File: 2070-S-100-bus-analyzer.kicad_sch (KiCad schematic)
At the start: 90 parts, among them J1 S-100 Edge Connector, J10 Conn_02x13_Odd_Even, J11 Conn_02x13_Odd_Even, J12 USB4105-GF-A, J13 Conn_01x01, J14 Conn_01x01, J15 Conn_01x02, J16 Conn_01x02, J17 Conn_01x02, J18 Conn_01x02, J19 Conn_01x02, J2 Conn_02x13_Odd_Even, J3 Conn_02x13_Odd_Even, J4 Conn_02x13_Odd_Even, J5 Conn_02x13_Odd_Even, J6 Conn_02x13_Odd_Even, J7 Conn_02x13_Odd_Even, J8 Conn_02x13_Odd_Even, J9 Conn_02x13_Odd_Even, SW1 SW_MEC_5E, U1 74LVCH245APW,118, U10 74LVCH245APW,118, U11 74LVCH245APW,118, U12 74LVCH245APW,118, U13 74LVCH245APW,118, U14 74LVCH245APW,118, U15 74LVCH245APW,118, U16 AP63300, U17 LMS78_05-2.0R, U2 74LVCH245APW,118, U3 74LVCH245APW,118, U4 74LVCH245APW,118, U5 74LVCH245APW,118, U6 74LVCH245APW,118, U7 74LVCH245APW,118, U8 74LVCH245APW,118, U9 74LVCH245APW,118

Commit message: Add some part info
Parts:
- R11: Digi-Key_PN (none) -> 311-2.20KHRCT-ND
- R4, R5: Digi-Key_PN (none) -> CR0603-FX-510ELFCT-ND
- TP1, TP2: Digi-Key_PN (none) -> 2019-RCWCTECT-ND
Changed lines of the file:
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@@
 			)
 		)
-		(property "Digi-Key_PN" ""
+		(property "Digi-Key_PN" "2019-RCWCTECT-ND"
 			(at 293.37 49.53 0)
 			(effects
@@
 			)
 		)
-		(property "Digi-Key_PN" ""
+		(property "Digi-Key_PN" "311-2.20KHRCT-ND"
 			(at 411.48 36.83 0)
 			(effects
@@
 			)
 		)
-		(property "Digi-Key_PN" ""
+		(property "Digi-Key_PN" "CR0603-FX-510ELFCT-ND"
 			(at 473.71 360.68 0)
 			(effects
@@
 			)
 		)
-		(property "Digi-Key_PN" ""
+		(property "Digi-Key_PN" "CR0603-FX-510ELFCT-ND"
 			(at 473.71 363.22 0)
 			(effects
@@
 			)
 		)
-		(property "Digi-Key_PN" ""
+		(property "Digi-Key_PN" "2019-RCWCTECT-ND"
 			(at 275.59 49.53 0)
 			(effects

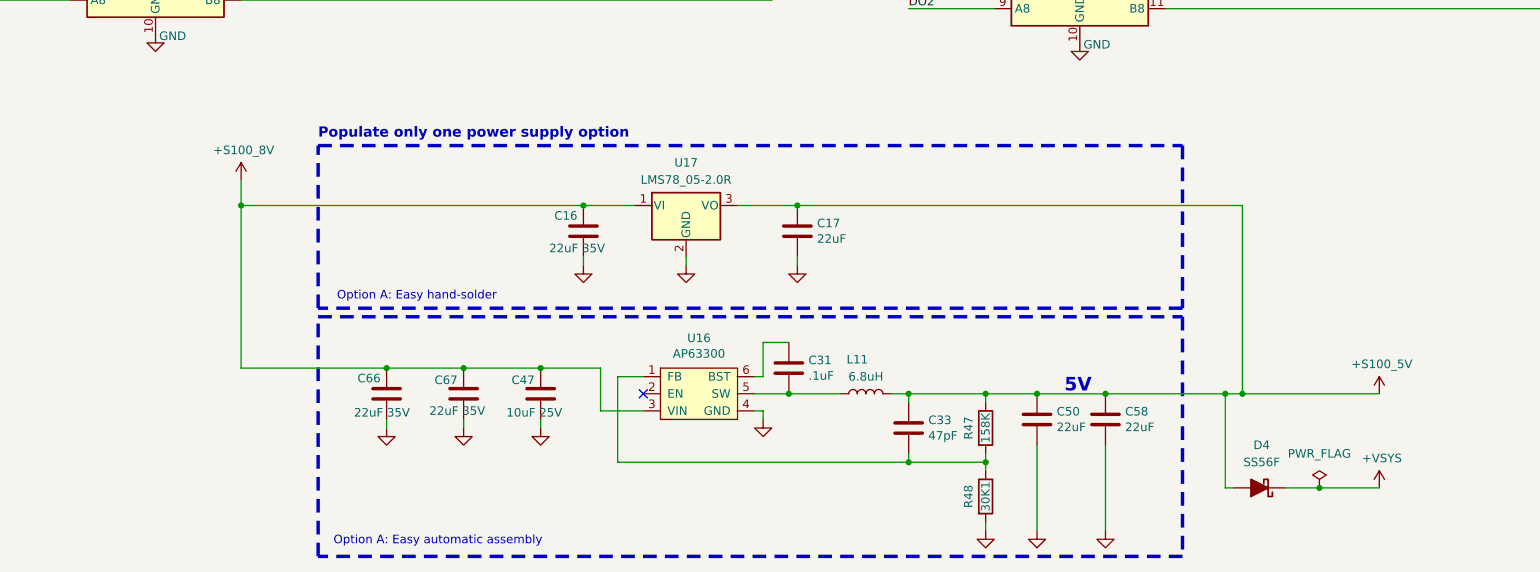
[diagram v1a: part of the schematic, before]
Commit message: Remove linear regulator option
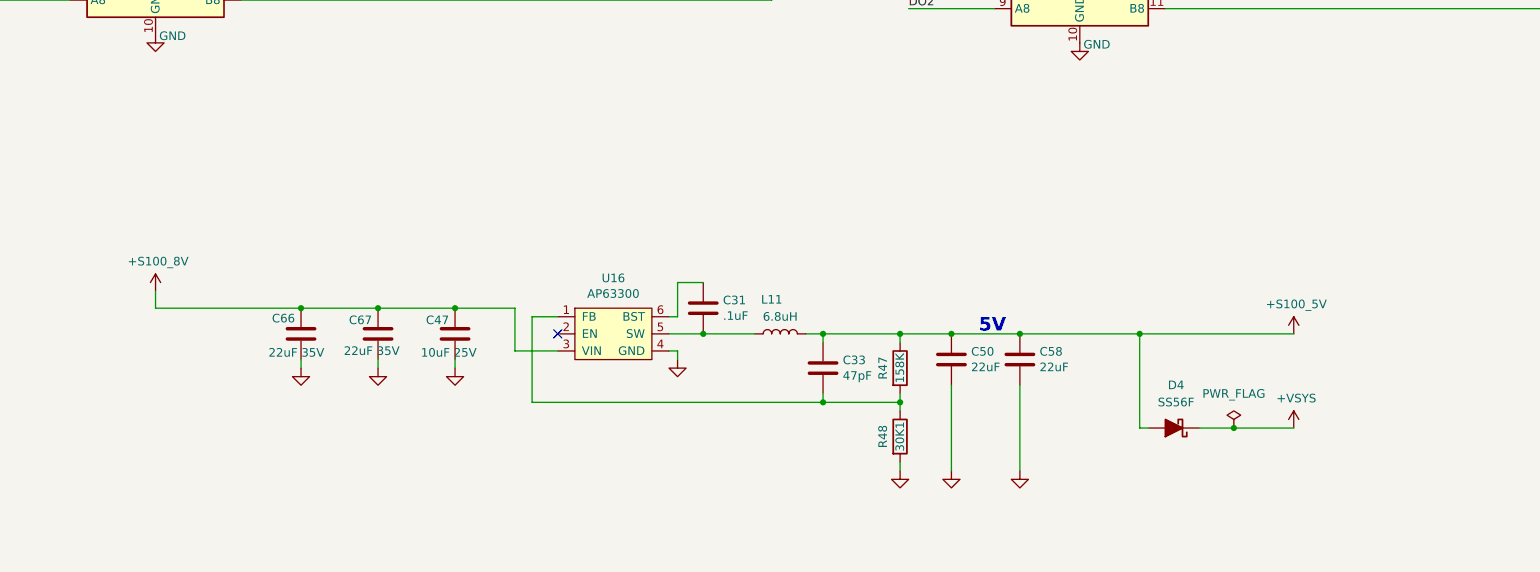
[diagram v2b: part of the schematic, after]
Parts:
- removed C16: 22uF 35V, Capacitor_SMD:C_0805_2012Metric_Pad1.18x1.45mm_HandSolder, symbol Device:C
- removed C17: 22uF, Capacitor_SMD:C_0805_2012Metric_Pad1.18x1.45mm_HandSolder, symbol Device:C
- removed U17: LMS78_05-2.0R, Package_TO_SOT_THT:TO-220-3_Horizontal_TabDown, symbol Regulator_Linear:LM7805_TO220
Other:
- note removed: "Option A: Easy automatic assembly"
- note removed: "Option A: Easy hand-solder"
- note removed: "Populate only one power supply option"
- moved on the sheet: C31, C33, C47, C50, C58, C66, C67, D4, L11, R47, R48, U16

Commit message: Add 3rd header row, note pins20/70, fonts, BOM
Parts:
- removed J13, J14: Conn_01x01, Connector_PinHeader_2.54mm:PinHeader_1x01_P2.54mm_Vertical, symbol Connector_Generic:Conn_01x01
- added J13, J14: Conn_01x02, Connector_PinHeader_2.54mm:PinHeader_1x02_P2.54mm_Vertical, symbol Connector_Generic:Conn_01x02
- added J22, J23, J24, J25, J26, J27, J28, J29: Conn_01x13, Connector_PinHeader_2.54mm:PinHeader_1x13_P2.54mm_Vertical, symbol Connector_Generic:Conn_01x13
- R11: MPN (none) -> RC0603FR-072K2L; Manufacturer (none) -> YAGEO
- R4, R5: MPN (none) -> CR0603-FX-5110ELF; Manufacturer (none) -> Bourns Inc.
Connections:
- net GND: now also J13.2 (Pin_2), J14.2 (Pin_2), J22.13 (Pin_13), J23.13 (Pin_13), J24.13 (Pin_13), J25.12 (Pin_12), J25.13 (Pin_13), J26.13 (Pin_13), J27.13 (Pin_13), J28.13 (Pin_13), J29.12 (Pin_12), J29.13 (Pin_13)
- net at J1.3 (XRDY), J2.1 (Pin_1): now also J22.1 (Pin_1)
- net at J1.8 (~{VI4}), J2.11 (Pin_11): now also J22.6 (Pin_6)
- net at J1.9 (~{VI5}), J2.13 (Pin_13): now also J22.7 (Pin_7)
- net at J1.10 (~{VI6}), J2.15 (Pin_15): now also J22.8 (Pin_8)
- net at J1.11 (~{VI7}), J2.17 (Pin_17): now also J22.9 (Pin_9)
- net at J1.12 (~{NMI}), J2.19 (Pin_19): now also J22.10 (Pin_10)
- net at J1.13 (~{PWRFAIL}), J2.21 (Pin_21): now also J22.11 (Pin_11)
- net at J1.14 (~{DMA3}), J2.23 (Pin_23): now also J22.12 (Pin_12)
- net at J1.4 (~{VI0}), J2.3 (Pin_3): now also J22.2 (Pin_2)
- net at J1.5 (~{VI1}), J2.5 (Pin_5): now also J22.3 (Pin_3)
- net at J1.6 (~{VI2}), J2.7 (Pin_7): now also J22.4 (Pin_4)
- net at J1.7 (~{VI3}), J2.9 (Pin_9): now also J22.5 (Pin_5)
- net at J1.15 (A18), J3.1 (Pin_1): now also J23.1 (Pin_1)
- net at J1.16 (A16), J3.3 (Pin_3): now also J23.2 (Pin_2)
- net at J1.17 (A17), J3.5 (Pin_5): now also J23.3 (Pin_3)
- net at J1.18 (~{SDSB}), J3.7 (Pin_7): now also J23.4 (Pin_4)
- net at J1.19 (~{CDSB}), J3.9 (Pin_9): now also J23.5 (Pin_5)
- net S100_20: now reaches J1.20 (GND), J3.11 (Pin_11)
- net S100_20: now also J14.1 (Pin_1), J23.6 (Pin_6)
- net at J1.21 (NDEF), J3.13 (Pin_13): now also J23.7 (Pin_7)
- net at J1.22 (~{ADSB}), J3.15 (Pin_15): now also J23.8 (Pin_8)
- net at J1.23 (~{DODSB}), J3.17 (Pin_17): now also J23.9 (Pin_9)
- net at J1.24 (PHI), J3.19 (Pin_19): now also J23.10 (Pin_10)
- net at J1.25 (~{pSTVAL}), J3.21 (Pin_21): now also J23.11 (Pin_11)
- net at J1.26 (pHLDA), J3.23 (Pin_23): now also J23.12 (Pin_12)
- net at J1.27 (RFU), J4.1 (Pin_1): now also J24.1 (Pin_1)
- net at J1.28 (RFU), J4.3 (Pin_3): now also J24.2 (Pin_2)
- net at J1.29 (A5), J4.5 (Pin_5): now also J24.3 (Pin_3)
- net at J1.30 (A4), J4.7 (Pin_7): now also J24.4 (Pin_4)
- net at J1.31 (A3), J4.9 (Pin_9): now also J24.5 (Pin_5)
- net at J1.32 (A15), J4.11 (Pin_11): now also J24.6 (Pin_6)
- net at J1.33 (A12), J4.13 (Pin_13): now also J24.7 (Pin_7)
- net at J1.34 (A9), J4.15 (Pin_15): now also J24.8 (Pin_8)
- net at J1.35 (DO1), J4.17 (Pin_17): now also J24.9 (Pin_9)
- net at J1.36 (DO0), J4.19 (Pin_19): now also J24.10 (Pin_10)
- net at J1.37 (A10), J4.21 (Pin_21): now also J24.11 (Pin_11)
- net at J1.38 (DO4), J4.23 (Pin_23): now also J24.12 (Pin_12)
- net at J1.39 (DO5), J5.1 (Pin_1): now also J25.1 (Pin_1)
- net at J1.40 (DO6), J5.3 (Pin_3): now also J25.2 (Pin_2)
- net at J1.41 (DI2), J5.5 (Pin_5): now also J25.3 (Pin_3)
- net at J1.42 (DI3), J5.7 (Pin_7): now also J25.4 (Pin_4)
- net at J1.43 (DI7), J5.9 (Pin_9): now also J25.5 (Pin_5)
- net at J1.44 (sM1), J5.11 (Pin_11): now also J25.6 (Pin_6)
- net at J1.45 (sOUT), J5.13 (Pin_13): now also J25.7 (Pin_7)
- net at J1.46 (sINP), J5.15 (Pin_15): now also J25.8 (Pin_8)
- net at J1.47 (sMEMR), J5.17 (Pin_17): now also J25.9 (Pin_9)
- net at J1.48 (sHLTA), J5.19 (Pin_19): now also J25.10 (Pin_10)
- net at J1.49 (CLOCK), J5.21 (Pin_21): now also J25.11 (Pin_11)
- net at J1.53 (GND), J6.1 (Pin_1): now also J26.1 (Pin_1)
- net at J1.54 (~{SLV_CLR}), J6.3 (Pin_3): now also J26.2 (Pin_2)
- net at J1.55 (~{DMA0}), J6.5 (Pin_5): now also J26.3 (Pin_3)
- net at J1.56 (~{DMA1}), J6.7 (Pin_7): now also J26.4 (Pin_4)
- net at J1.57 (~{DMA2}), J6.9 (Pin_9): now also J26.5 (Pin_5)
- net at J1.58 (~{sXTRQ}), J6.11 (Pin_11): now also J26.6 (Pin_6)
- net at J1.59 (A19), J6.13 (Pin_13): now also J26.7 (Pin_7)
- net at J1.60 (~{SIXTN}), J6.15 (Pin_15): now also J26.8 (Pin_8)
- net at J1.61 (A20), J6.17 (Pin_17): now also J26.9 (Pin_9)
- net at J1.62 (A21), J6.19 (Pin_19): now also J26.10 (Pin_10)
- net at J1.63 (A22), J6.21 (Pin_21): now also J26.11 (Pin_11)
- net at J1.64 (A23), J6.23 (Pin_23): now also J26.12 (Pin_12)
- net at J1.65 (NDEF), J7.1 (Pin_1): now also J27.1 (Pin_1)
- net at J1.66 (NDEF), J7.3 (Pin_3): now also J27.2 (Pin_2)
- net at J1.67 (~{PHANTOM}), J7.5 (Pin_5): now also J27.3 (Pin_3)
- net at J1.68 (MWRT), J7.7 (Pin_7): now also J27.4 (Pin_4)
- net at J1.69 (RFU), J7.9 (Pin_9): now also J27.5 (Pin_5)
- net S100_70: now reaches J1.70 (GND), J7.11 (Pin_11)
- net S100_70: now also J13.1 (Pin_1), J27.6 (Pin_6)
- net at J1.71 (RFU), J7.13 (Pin_13): now also J27.7 (Pin_7)
- net at J1.72 (RDY), J7.15 (Pin_15): now also J27.8 (Pin_8)
- net at J1.73 (~{INT}), J7.17 (Pin_17): now also J27.9 (Pin_9)
- net at J1.74 (~{HOLD}), J7.19 (Pin_19): now also J27.10 (Pin_10)
- net at J1.75 (~{RESET}), J7.21 (Pin_21): now also J27.11 (Pin_11)
- net at J1.76 (pSYNC), J7.23 (Pin_23): now also J27.12 (Pin_12)
- net at J1.77 (~{pWR}), J8.1 (Pin_1): now also J28.1 (Pin_1)
- net at J1.78 (pDBIN), J8.3 (Pin_3): now also J28.2 (Pin_2)
- net at J1.79 (A0), J8.5 (Pin_5): now also J28.3 (Pin_3)
- net at J1.80 (A1), J8.7 (Pin_7): now also J28.4 (Pin_4)
- net at J1.81 (A2), J8.9 (Pin_9): now also J28.5 (Pin_5)
- net at J1.82 (A6), J8.11 (Pin_11): now also J28.6 (Pin_6)
- net at J1.83 (A7), J8.13 (Pin_13): now also J28.7 (Pin_7)
- net at J1.84 (A8), J8.15 (Pin_15): now also J28.8 (Pin_8)
- net at J1.85 (A13), J8.17 (Pin_17): now also J28.9 (Pin_9)
- net at J1.86 (A14), J8.19 (Pin_19): now also J28.10 (Pin_10)
- net at J1.87 (A11), J8.21 (Pin_21): now also J28.11 (Pin_11)
- net at J1.88 (DO2), J8.23 (Pin_23): now also J28.12 (Pin_12)
- net at J1.89 (DO3), J9.1 (Pin_1): now also J29.1 (Pin_1)
- net at J1.90 (DO7), J9.3 (Pin_3): now also J29.2 (Pin_2)
- net at J1.91 (DI4), J9.5 (Pin_5): now also J29.3 (Pin_3)
- net at J1.92 (DI5), J9.7 (Pin_7): now also J29.4 (Pin_4)
- net at J1.93 (DI6), J9.9 (Pin_9): now also J29.5 (Pin_5)
- net at J1.94 (DI1), J9.11 (Pin_11): now also J29.6 (Pin_6)
- net at J1.95 (DI0), J9.13 (Pin_13): now also J29.7 (Pin_7)
- net at J1.96 (sINTA), J9.15 (Pin_15): now also J29.8 (Pin_8)
- net at J1.97 (~{sWO}), J9.17 (Pin_17): now also J29.9 (Pin_9)
- net at J1.98 (~{ERROR}), J9.19 (Pin_19): now also J29.10 (Pin_10)
- net at J1.99 (~{POC}), J9.21 (Pin_21): now also J29.11 (Pin_11)
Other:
- moved on the sheet: J2, J3, J4, J5, J6, J7, J8, J9
